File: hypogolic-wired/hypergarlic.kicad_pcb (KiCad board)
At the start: 2 copper layers, 237.8 x 87.7 mm, 49 parts, among them J1 AudioJack4dpb, J2 AudioJack4dpb, SW10 SW_Push, SW11 SW_Push, SW11_r1 SW_Push, SW12 SW_Push, SW12_r1 SW_Push, SW13_r1 SW_Push, SW14 SW_Push, SW15 SW_Push, SW15_r1 SW_Push, SW16 SW_Push, SW16_r1 SW_Push, SW17 SW_Push, SW17_r1 SW_Push, SW18 SW_Push, SW18_r1 SW_Push, SW2 SW_Push, SW20 SW_Push, SW20_r1 SW_Push, SW21 SW_Push, SW21_r1 SW_Push, SW2_r1 SW_Push, SW3 SW_Push, SW3_r1 SW_Push, SW4 SW_Push, SW4_r1 SW_Push, SW5 SW_Push, SW5_r1 SW_Push, SW6 SW_Push, SW6_r1 SW_Push, SW7_r1 SW_Push, SW8 SW_Push, SW8_r1 SW_Push, SW9 SW_Push, SW9_r1 SW_Push, U1 ProMicro-kbd, U2 ProMicro-kbd

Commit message: fill
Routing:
- net Switch15: track 44.7 -> 41.7 mm
- net Switch11: track 144.1 -> 146.9 mm
- net Switch14: track 72.2 -> 69.4 mm
- net Switch12: track 114.8 -> 117.5 mm
- net Switch13: track 91.9 -> 94.6 mm
- net Switch16: track 55.2 -> 52.7 mm

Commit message: move apart a bit
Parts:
- moved Bat+1 1.00 mm to (139.4, 44.7)
- moved BatGND4 1.00 mm to (150.6, 44.7)
- moved G*** 1.00 mm to (195.8, 97.0)
- moved J1 1.00 mm to (138.7, 80.2)
- moved REF** 1.00 mm to (190.5, 52.1)
- moved RSW2 1.00 mm to (169.9, 33.8)
- moved SW11_r1 1.00 mm to (181.5, 58.7)
- moved SW12_r1 1.00 mm to (163.5, 61.2)
- moved SW13_r1 1.00 mm to (233.0, 95.2)
- moved SW15_r1 1.00 mm to (199.5, 70.4)
- moved SW16_r1 1.00 mm to (181.5, 75.7)
- moved SW17_r1 1.00 mm to (163.5, 78.2)
- moved SW18_r1 1.00 mm to (217.9, 76.4)
- moved SW20_r1 1.00 mm to (145.0, 97.5)
- moved SW2_r1 1.00 mm to (241.8, 62.4)
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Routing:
- net gnd: track 8.45 -> 9.45 mm
- net vcc: track 92.4 -> 93.4 mm
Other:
- board size 237.8 x 87.7 mm -> 238.8 x 87.7 mm

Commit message: Add files via upload
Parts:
- added mouse-bite-2mm-slot: VAL**, kbd:mouse-bite-2mm-slot-with-space-for-track, F.Cu at (134.6, 50.0)
- added mouse-bite-2mm-slot: VAL**, kbd:mouse-bite-2mm-slot-with-space-for-track, F.Cu at (134.6, 81.5)
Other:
- outline, holes or cut-outs redrawn

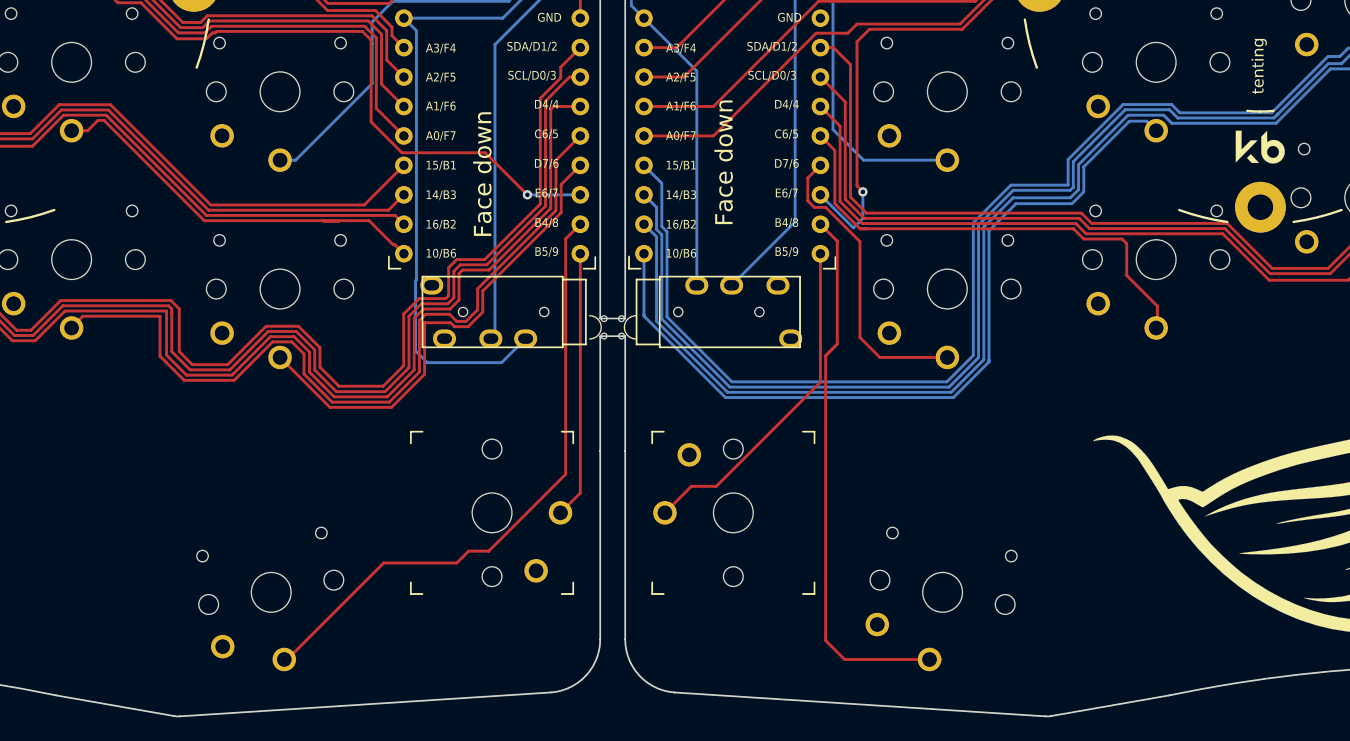
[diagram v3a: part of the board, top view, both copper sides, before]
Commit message: move trrs things, make effort at actual symmetry
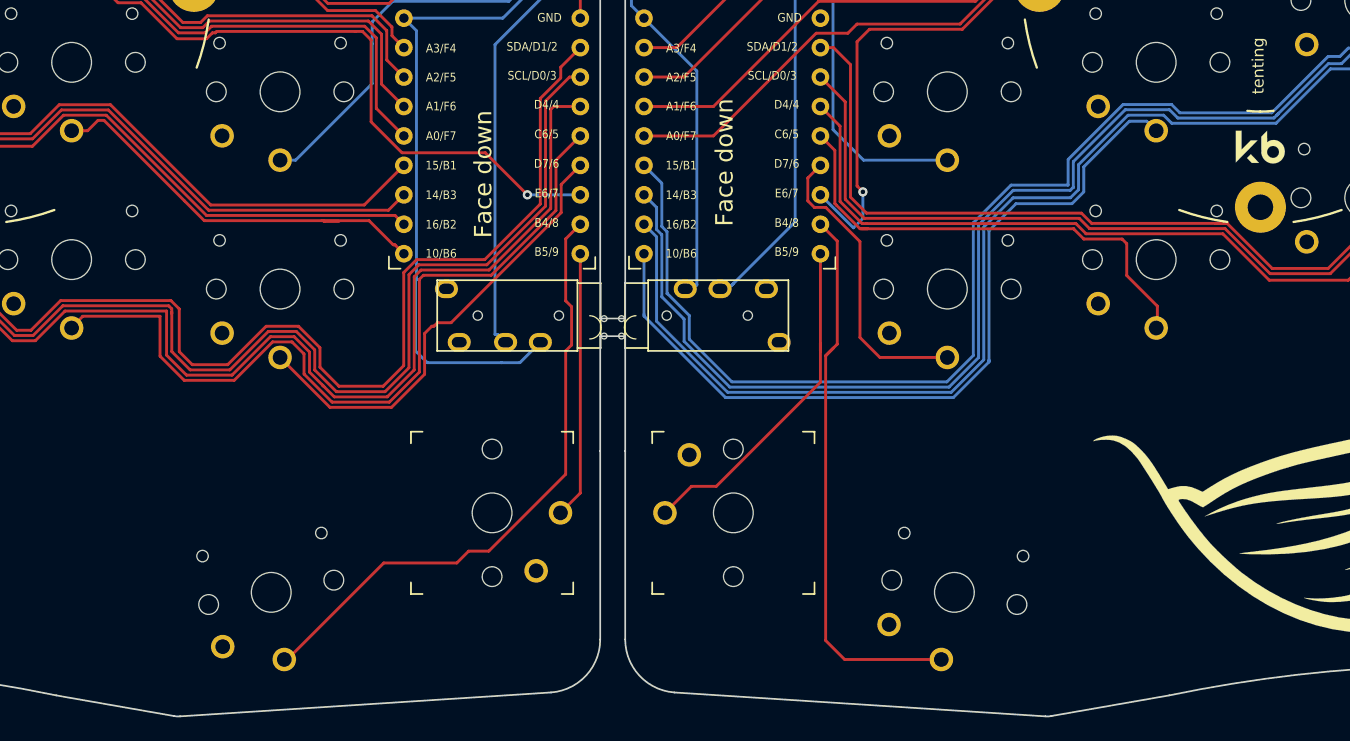
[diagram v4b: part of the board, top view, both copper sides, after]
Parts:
- moved J2 1.31 mm to (131.6, 80.5)
- moved J1 1.05 mm to (137.7, 80.5)
- moved SW21_r1 1.02 mm to (164.1, 104.4)
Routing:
- net vcc: track 93.4 -> 95.7 mm
- net Switch15: track 41.7 -> 39.8 mm
- net Switch18_r: track 31.3 -> 32.7 mm
- net Switch13: track 94.6 -> 95.4 mm
- net Switch12: track 117.5 -> 118.3 mm
- net Switch11: track 146.9 -> 147.5 mm
- net Switch18: track 35.9 -> 36.6 mm
- net Switch14: track 69.4 -> 69.9 mm
